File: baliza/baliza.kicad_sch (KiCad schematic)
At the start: 19 parts

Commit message: updates
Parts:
- removed A?: Arduino_Nano_v2.x, Module:Arduino_Nano, symbol MCU_Module:Arduino_Nano_v2.x
- added A1: Arduino_Nano_v3.x, Module:Arduino_Nano, symbol MCU_Module:Arduino_Nano_v3.x
- added J1: ALIMENTACION, TerminalBlock_RND:TerminalBlock_RND_205-00001_1x02_P5.00mm_Horizontal, symbol Connector:Conn_01x02_Male
- added J2: PTT, TerminalBlock_RND:TerminalBlock_RND_205-00001_1x02_P5.00mm_Horizontal, symbol Connector:Conn_01x02_Male
- added J3: AUDIO, TerminalBlock_RND:TerminalBlock_RND_205-00001_1x02_P5.00mm_Horizontal, symbol Connector:Conn_01x02_Male
- added J4: VCC_13v8_ENTRADA, TerminalBlock_RND:TerminalBlock_RND_205-00001_1x02_P5.00mm_Horizontal, symbol Connector:Conn_01x02_Male
- C1, C4: renamed from C?; footprint (none) -> Capacitor_THT:CP_Radial_D5.0mm_P2.00mm
- C2, C3, C5: renamed from C?; footprint (none) -> Capacitor_THT:C_Disc_D4.7mm_W2.5mm_P5.00mm
- JP1, JP2, JP3: renamed from JP?; footprint (none) -> Connector_PinHeader_2.54mm:PinHeader_1x02_P2.54mm_Vertical
- JP4: renamed from JP?; footprint (none) -> Jumper:SolderJumper-2_P1.3mm_Open_RoundedPad1.0x1.5mm
- R1, R2: renamed from R?; footprint (none) -> Resistor_THT:R_Axial_DIN0204_L3.6mm_D1.6mm_P5.08mm_Horizontal
- U1: renamed from U?; footprint (none) -> Package_TO_SOT_THT:TO-220-3_Vertical
- gave numbers to parts that had none: 6
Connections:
- net VPP is gone; now on net VCC: C1.1, C2.1, U1.1 (IN)
- net +5V: now also A1.27 (+5V)
- net ENTRADA_AUDIO_MIC: now also J3.2 (Pin_2)
- net GND: now also A1.29 (GND), A1.4 (GND), J1.1 (Pin_1), J2.2 (Pin_2), J3.1 (Pin_1), J4.1 (Pin_1)
- net PTT_TRANSCEPTOR: now also J2.1 (Pin_1)
- net Rele encendido: now also A1.5 (D2)
- net VCC: now also J1.2 (Pin_2)
- net VCC_13v8_ENTRADA: now also J4.2 (Pin_2)
- net at JP3.2 (B): now also A1.15 (D12)
- net at JP1.2 (B): now also A1.13 (D10)
- net at R2.2: now also A1.10 (D7)
- net at JP2.2 (B): now also A1.14 (D11)
- net at JP4.1 (A): now also A1.3 (~{RESET})
- net at C3.2: now also A1.9 (D6)
- no-connect marks 21 -> 22
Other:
- moved on the sheet: C1, C2, C4, C5, U1

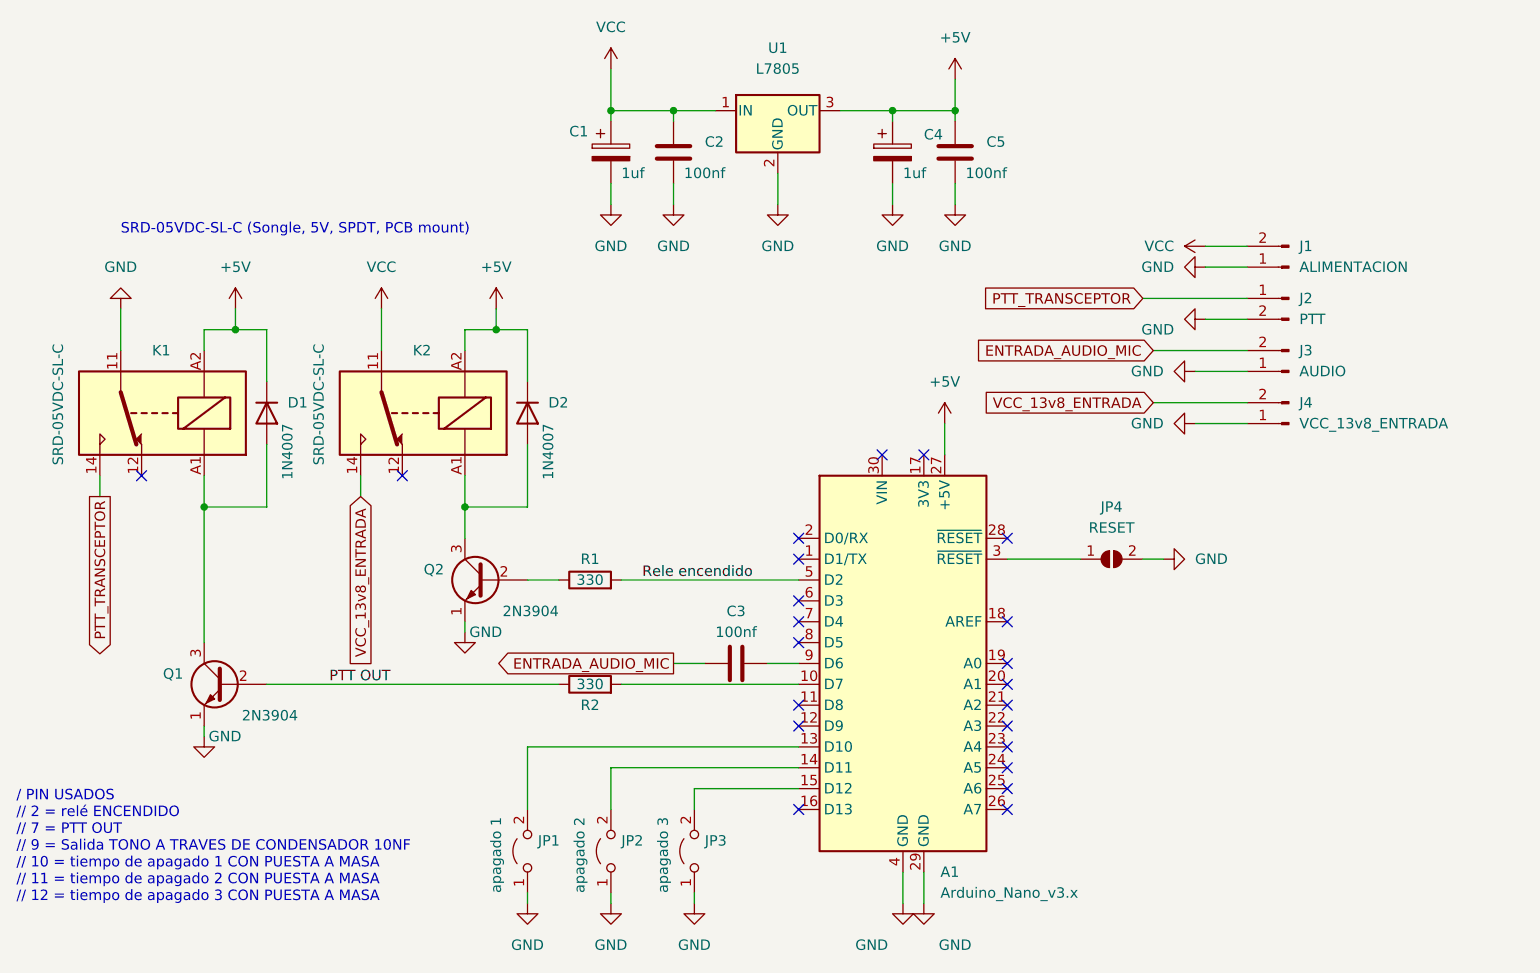
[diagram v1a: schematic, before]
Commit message: anadir LEDs auxiliares, pistas en cara inferior
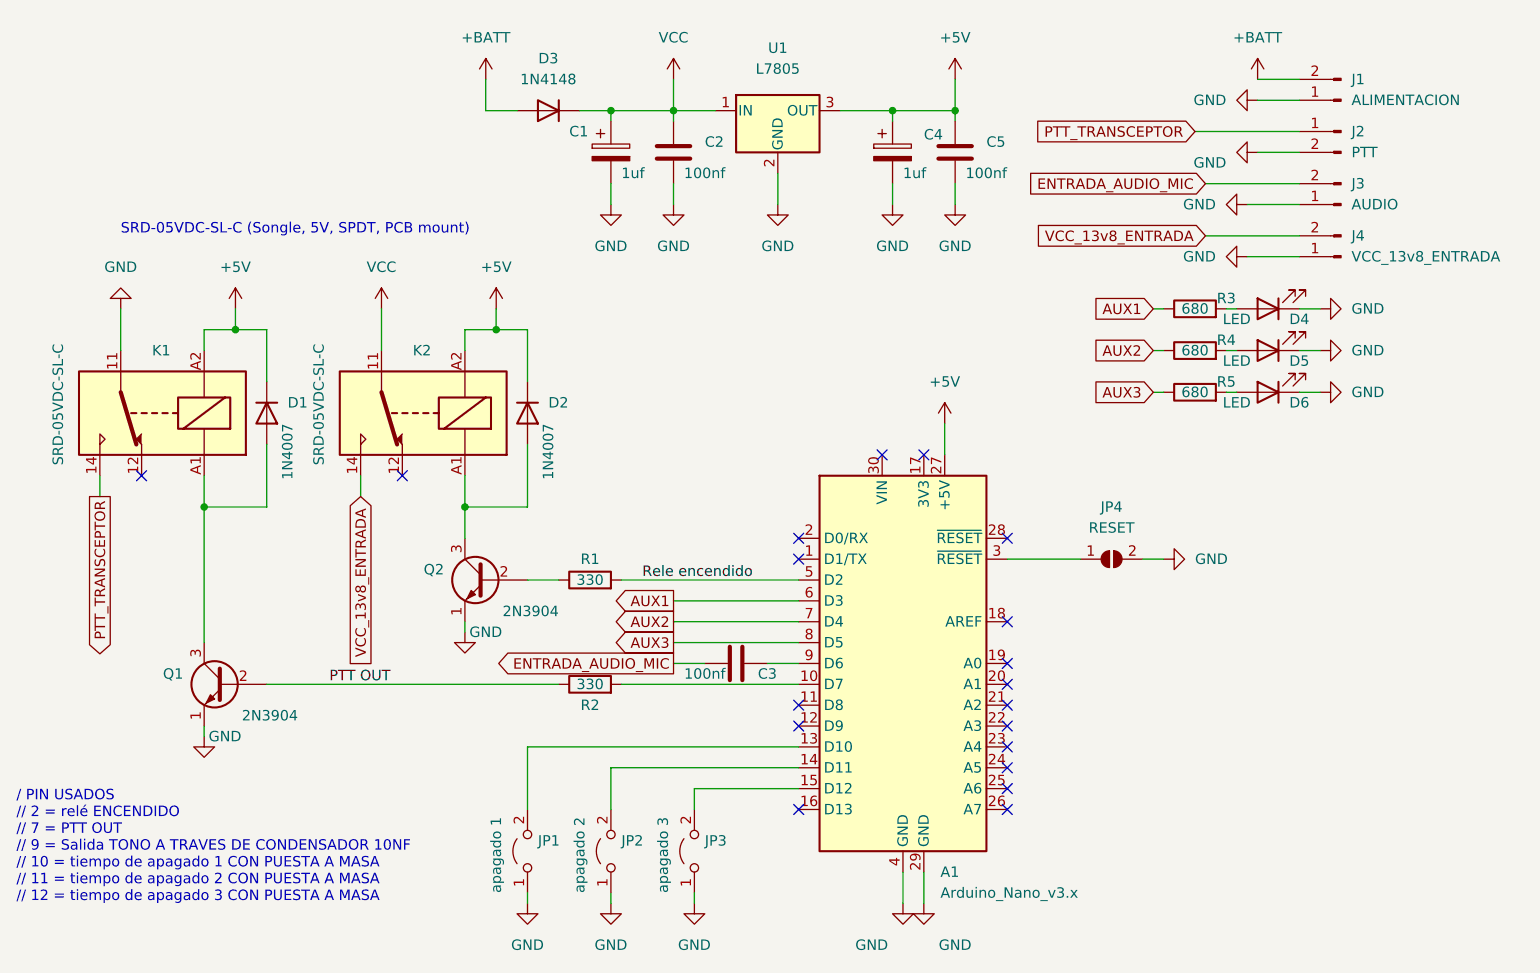
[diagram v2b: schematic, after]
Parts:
- added D3: 1N4148, Diode_THT:D_DO-35_SOD27_P7.62mm_Horizontal, symbol Diode:1N4148
- added D4, D5, D6: LED, LED_THT:LED_D5.0mm, symbol Device:LED
- added R3, R4, R5: 680, Resistor_THT:R_Axial_DIN0204_L3.6mm_D1.6mm_P5.08mm_Horizontal, symbol Device:R
- JP4: footprint Jumper:SolderJumper-2_P1.3mm_Open_RoundedPad1.0x1.5mm -> Connector_PinHeader_2.54mm:PinHeader_1x02_P2.54mm_Vertical
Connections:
- net GND: now also D4.1 (K), D5.1 (K), D6.1 (K)
- net VCC: now also D3.1 (K); no longer J1.2 (Pin_2)
- net AUX1: now reaches A1.6 (D3)
- net AUX1: now also R3.1
- net AUX2: now reaches A1.7 (D4)
- net AUX2: now also R4.1
- net AUX3: now reaches A1.8 (D5)
- net AUX3: now also R5.1
- new net: D6.2 (A), R5.2
- new net: D5.2 (A), R4.2
- new net: D4.2 (A), R3.2
- new net +BATT: D3.2 (A), J1.2 (Pin_2)
- no-connect marks 22 -> 19
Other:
- moved on the sheet: J1, J2, J3, J4
